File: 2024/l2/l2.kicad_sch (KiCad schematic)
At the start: 6 parts, among them J1 Conn_01x04, J2 Conn_01x02, J3 Conn_01x04, U1 DEV-15583, U2 VNH5019A-E, U3 TLP175A

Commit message: Motor Driver sch very wonky draft
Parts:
- removed U3: TLP175A, Package_SO:MFSOP6-4_4.4x3.6mm_P1.27mm, symbol Relay_SolidState:TLP175A
- added Q1: IRF540N, Package_TO_SOT_THT:TO-220-3_Vertical, symbol Transistor_FET:IRF540N
- added R1, R2, R3, R4, R7: 1k, symbol Device:R
- added R5, R6: 3.3k, symbol Device:R
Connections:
- net +12V: now also U2.12 (VBAT), Q1.2 (D)
- net +5V: now also R5.2, R6.2
- net PWM: now reaches U1.2
- net PWM: now also R1.1
- net INA: now reaches U1.3
- net INA: now also R3.1
- net INB: now reaches U1.4
- net INB: now also R2.1
- net at U1.5: now also R4.2
- net at U1.6: now also R7.2
- net at U2.10 (INB): now also R2.2
- net CP: now reaches U2.11 (CP)
- net CP: now also Q1.1 (G)
- net at U2.13 (VCC), U2.23 (VCC), U2.3 (VCC)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: now also Q1.3 (S)
- net at U2.4 (INA): now also R3.2
- net ENA: now reaches U2.5 (EN/DIAGA)
- net ENA: now also R4.1, R5.1
- net at U2.7 (PWM): now also R1.2
- net ENB: now reaches U2.9 (EN/DIAGB)
- net ENB: now also R6.1, R7.1

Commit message: 26/7 final
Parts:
- R4: value 1k -> 3.3k
- R5: value 3.3k -> 1k
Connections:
- net +5V: now also R4.2; no longer R5.2
- net ENA: now also R5.2; no longer R5.1
- net ENB: now also R7.2; no longer R7.1
- net GND: now also Q1.3 (S), R5.1, R7.1, U2.13 (VCC), U2.23 (VCC), U2.3 (VCC), U2.31 (VCC)
- net at U1.5: no longer R4.2
- net at U1.6: no longer R7.2
- no-connect marks 0 -> 2

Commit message: 31/7 final
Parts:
- added C1: 680uF, symbol Device:C_Polarized
- added M1: Motor_DC, symbol Motor:Motor_DC
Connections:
- net +5V: now also Q1.3 (S), U2.13 (VCC), U2.23 (VCC), U2.3 (VCC), U2.31 (VCC), C1.1; no longer R4.2, R6.2
- net GND: now also C1.2; no longer Q1.3 (S), U2.13 (VCC), U2.23 (VCC), U2.3 (VCC), U2.31 (VCC)
- net at U2.1 (OUTA), U2.25 (OUTA), U2.30 (OUTA)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: now also M1.1 (+)
- net at U2.15 (OUTB), U2.16 (OUTB), U2.21 (OUTB)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: now also M1.2 (-)
- new net: R4.2, R6.2
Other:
- moved on the sheet: J1, J2, J3, Q1, R1, R2, R3, R4, R5, R6, R7, U2

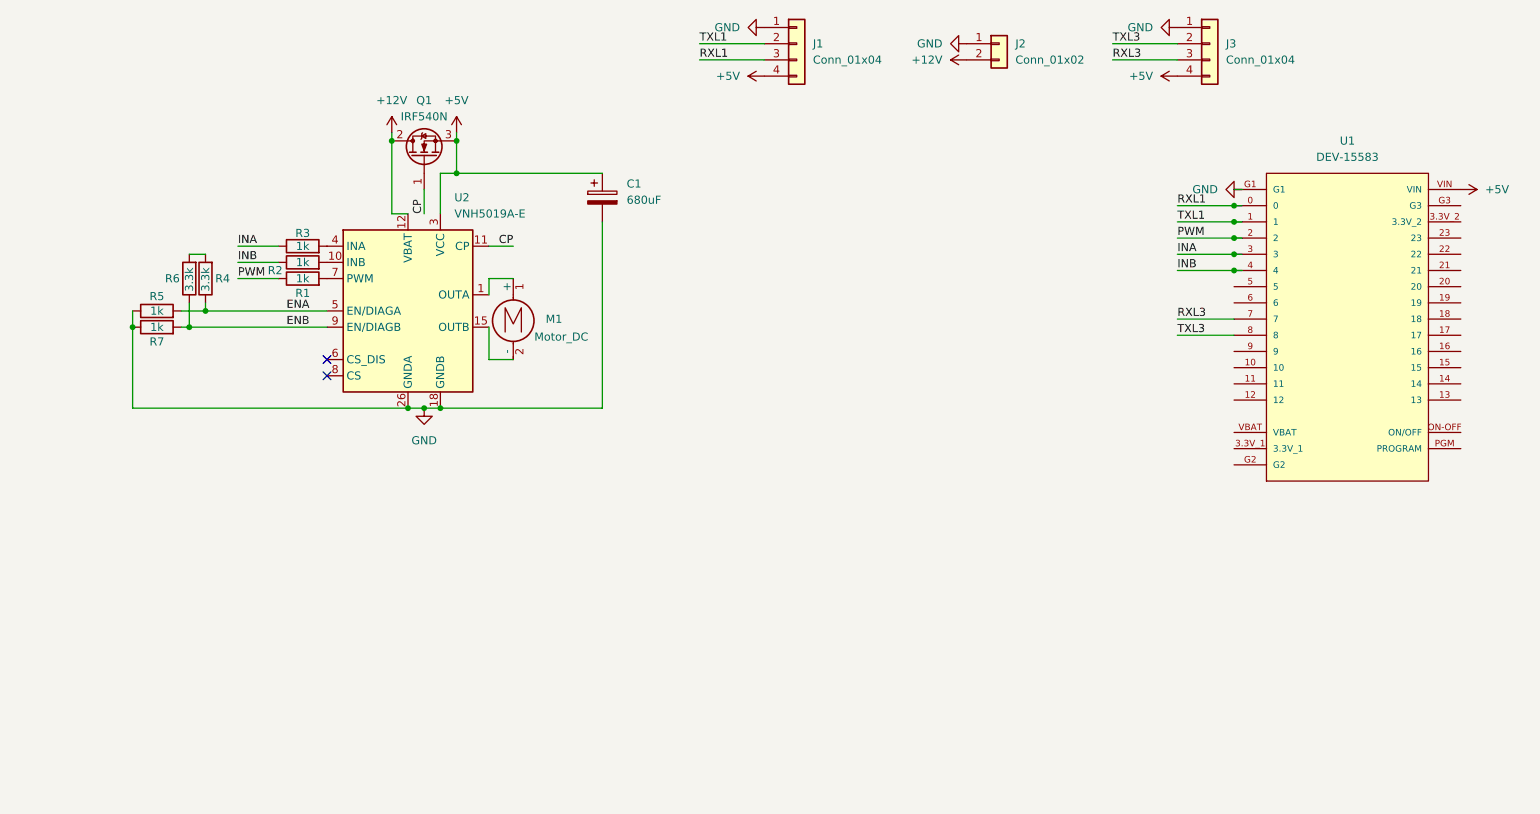
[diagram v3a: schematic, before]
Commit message: Refined motor driver schematics
L2 schematics basically good to go might need final senior's review
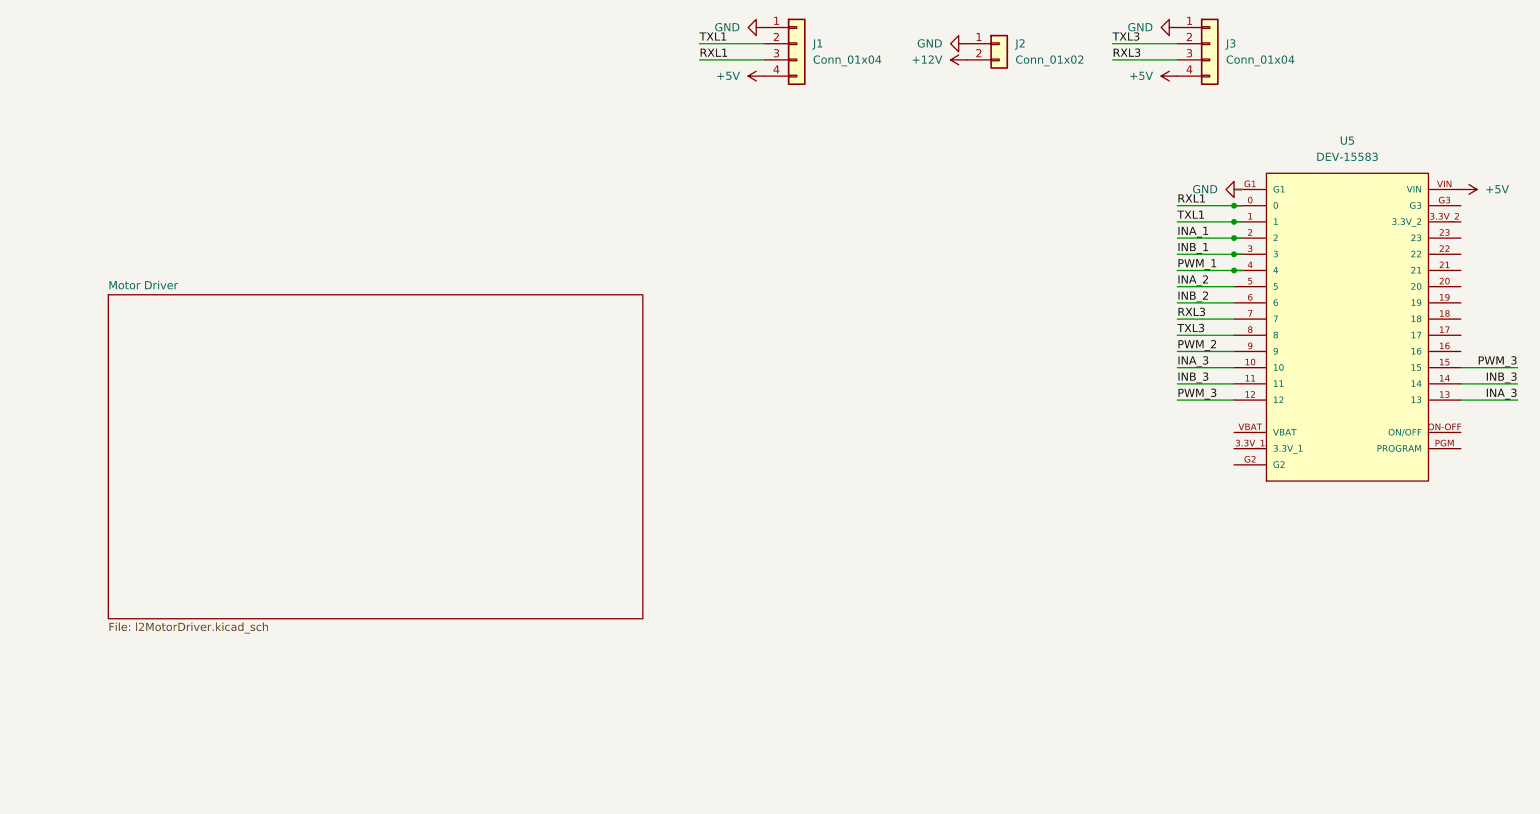
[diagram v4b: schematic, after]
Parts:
- removed C1: 680uF, symbol Device:C_Polarized
- removed M1: Motor_DC, symbol Motor:Motor_DC
- removed Q1: IRF540N, Package_TO_SOT_THT:TO-220-3_Vertical, symbol Transistor_FET:IRF540N
- removed R1, R2, R3, R5, R7: 1k, symbol Device:R
- removed R4, R6: 3.3k, symbol Device:R
- removed U2: VNH5019A-E, Package_SO:ST_MultiPowerSO-30, symbol Driver_Motor:VNH5019A-E
- renumbered U1 to U5
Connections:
- net INA_3: now reaches U5.10
- net INA_3: now also U5.13
- net INB_3: now reaches U5.11
- net INB_3: now also U5.14
- net PWM_3: now reaches U5.12
- net PWM_3: now also U5.15
- net INA_2: now reaches U5.5
- net INB_2: now reaches U5.6
- net PWM_2: now reaches U5.9
- net INA renamed INB_1
- net INB renamed PWM_1
- net PWM renamed INA_1
- no-connect marks 2 -> 0
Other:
- added sheet Motor Driver (l2MotorDriver.kicad_sch)

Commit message: 7/8 part_I
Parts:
- U5: footprint DEV-15583:MODULE_DEV-15583 -> Board:MODULE_DEV-15583
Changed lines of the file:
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@@
 			)
 		)
-		(property "Footprint" "DEV-15583:MODULE_DEV-15583"
+		(property "Footprint" "Board:MODULE_DEV-15583"
 			(at 220.98 64.77 0)
 			(effects

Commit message: 14/8 final
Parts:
- added H1, H10, H11, H12, H13, H14, H15, H16, H2, H3, H4, H5, H6, H7, H8, H9: MountingHole_Pad, MountingHole:MountingHole_3.2mm_M3_Pad_Via, symbol Mechanical:MountingHole_Pad
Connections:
- no-connect marks 0 -> 16

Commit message: 16/8 final
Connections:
- net PWM_1 renamed PWM_!
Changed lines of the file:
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@@
 	(generator_version "8.0")
 	(paper "A4")
-	(junction
-		(at 203.2 52.07)
-		(diameter 0)
-		(color 0 0 0 0)
-	)
-	(junction
-		(at 203.2 49.53)
-		(diameter 0)
-		(color 0 0 0 0)
-	)
-	(junction
-		(at 203.2 46.99)
-		(diameter 0)
-		(color 0 0 0 0)
-	)
-	(junction
-		(at 203.2 57.15)
-		(diameter 0)
-		(color 0 0 0 0)
-	)
-	(junction
-		(at 203.2 54.61)
-		(diameter 0)
-		(color 0 0 0 0)
-	)
 	(no_connect
 		(at 222.25 139.7)
@@
 	(wire
 		(pts
-			(xy 204.47 49.53) (xy 203.2 49.53)
-		)
-		(stroke
-			(width 0)
-			(type default)
-		)
-	)
-	(wire
-		(pts
 			(xy 247.65 77.47) (xy 238.76 77.47)
 		)
@@
 	(wire
 		(pts
-			(xy 204.47 57.15) (xy 203.2 57.15)
-		)
-		(stroke
-			(width 0)
-			(type default)
-		)
-	)
-	(wire
-		(pts
-			(xy 204.47 54.61) (xy 203.2 54.61)
-		)
-		(stroke
-			(width 0)
-			(type default)
-		)
-	)
-	(wire
-		(pts
 			(xy 194.31 54.61) (xy 203.2 54.61)
 		)
@@
 	(wire
 		(pts
-			(xy 204.47 46.99) (xy 203.2 46.99)
-		)
-		(stroke
-			(width 0)
-			(type default)
-		)
-	)
-	(wire
-		(pts
 			(xy 194.31 67.31) (xy 203.2 67.31)
 		)
@@
 		(pts
 			(xy 194.31 77.47) (xy 203.2 77.47)
-		)
-		(stroke
-			(width 0)
-			(type default)
-		)
-	)
-	(wire
-		(pts
-			(xy 204.47 52.07) (xy 203.2 52.07)
-		)
-		(stroke
-			(width 0)
-			(type default)
-		)
-	)
-	(wire
-		(pts
-			(xy 194.31 57.15) (xy 203.2 57.15)
 		)
 		(stroke
@@
 		)
 	)
-	(label "PWM_1"
-		(at 194.31 57.15 0)
-		(fields_autoplaced yes)
-		(effects
-			(font
-				(size 1.27 1.27)
-			)
-			(justify left bottom)
-		)
-	)
 	(label "INB_2"
 		(at 194.31 62.23 0)
@@
 		)
 	)
+	(hierarchical_label "PWM_!"
+		(shape input)
+		(at 203.2 57.15 180)
+		(fields_autoplaced yes)
+		(effects
+			(font
+				(size 1.27 1.27)
+			)
+			(justify right)
+		)
+	)

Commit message: 21/8 final
about 10% done l2 pcb
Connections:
- net INA_3: no longer U5.13
- net INB_3: no longer U5.14
- net PWM_3: no longer U5.15
- net PWM_! renamed PWM_1
- new net INA_4: U5.13
- new net INB_4: U5.14
- new net PWM_4: U5.15
